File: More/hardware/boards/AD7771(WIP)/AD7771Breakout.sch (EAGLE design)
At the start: 44 parts, among them U1 AD7771BCPZ, U2 MAX6070AAUT25T, U3 LP5907MFX-3.3/NOPB, U4 TBA1-0310, U5 SG-210STF8.1920ML3, X1 332-02

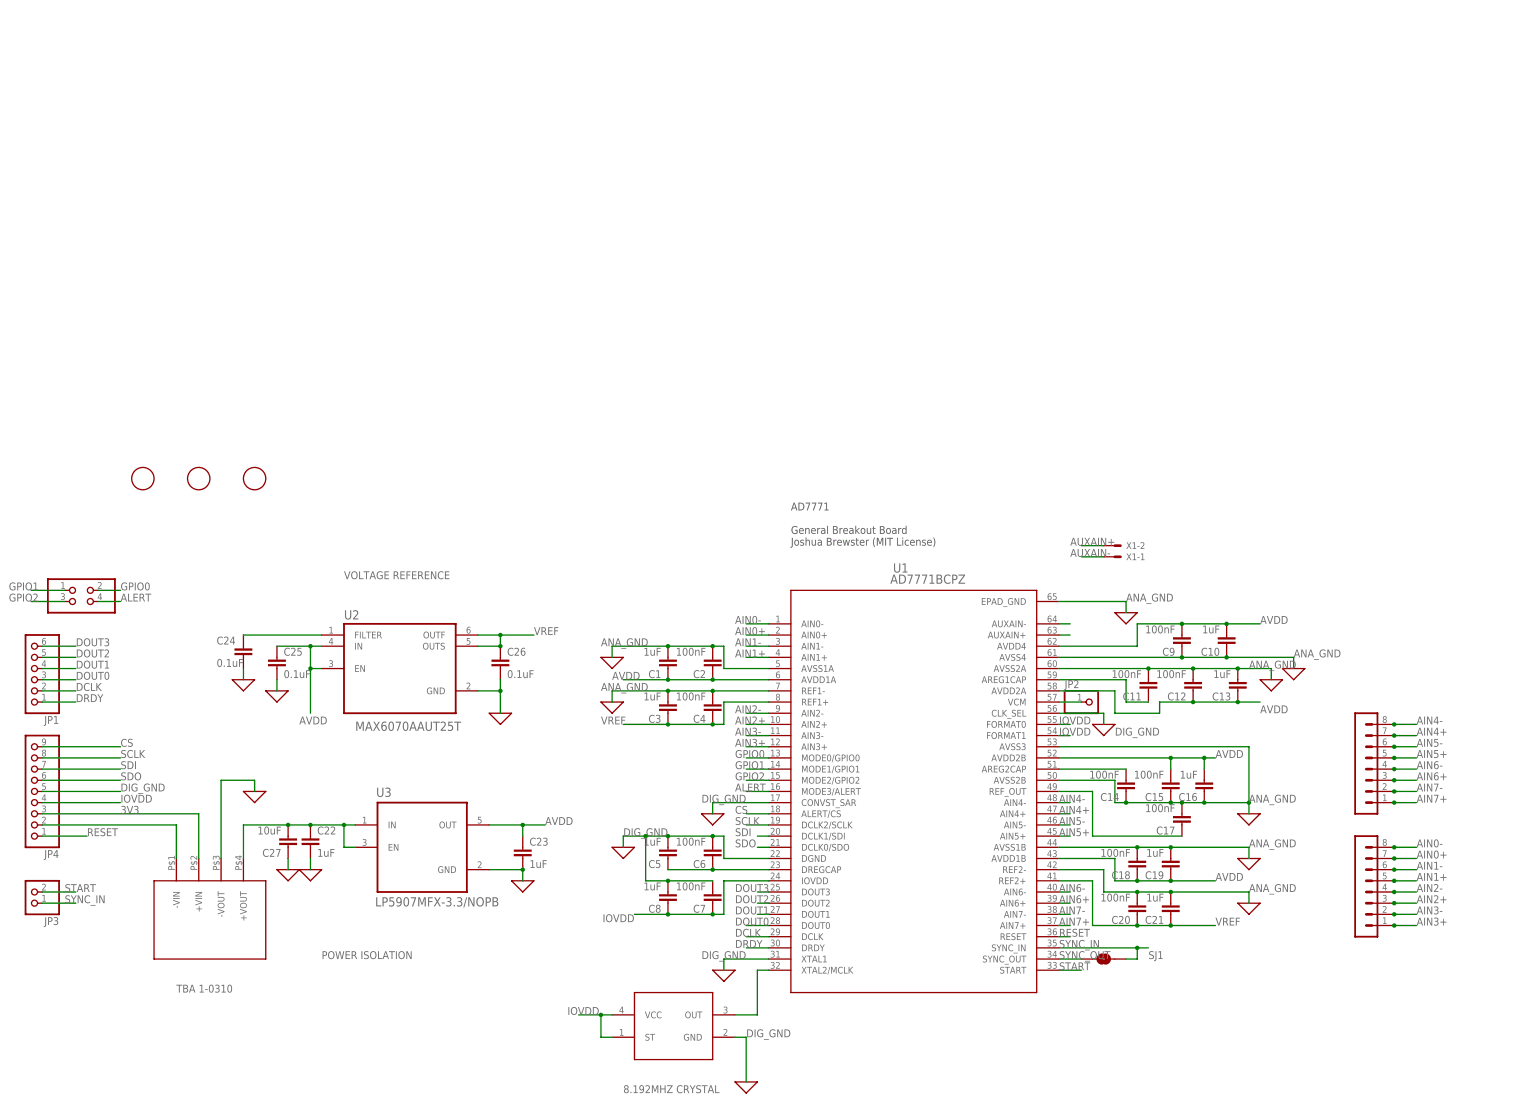
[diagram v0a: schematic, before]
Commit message: update schematic
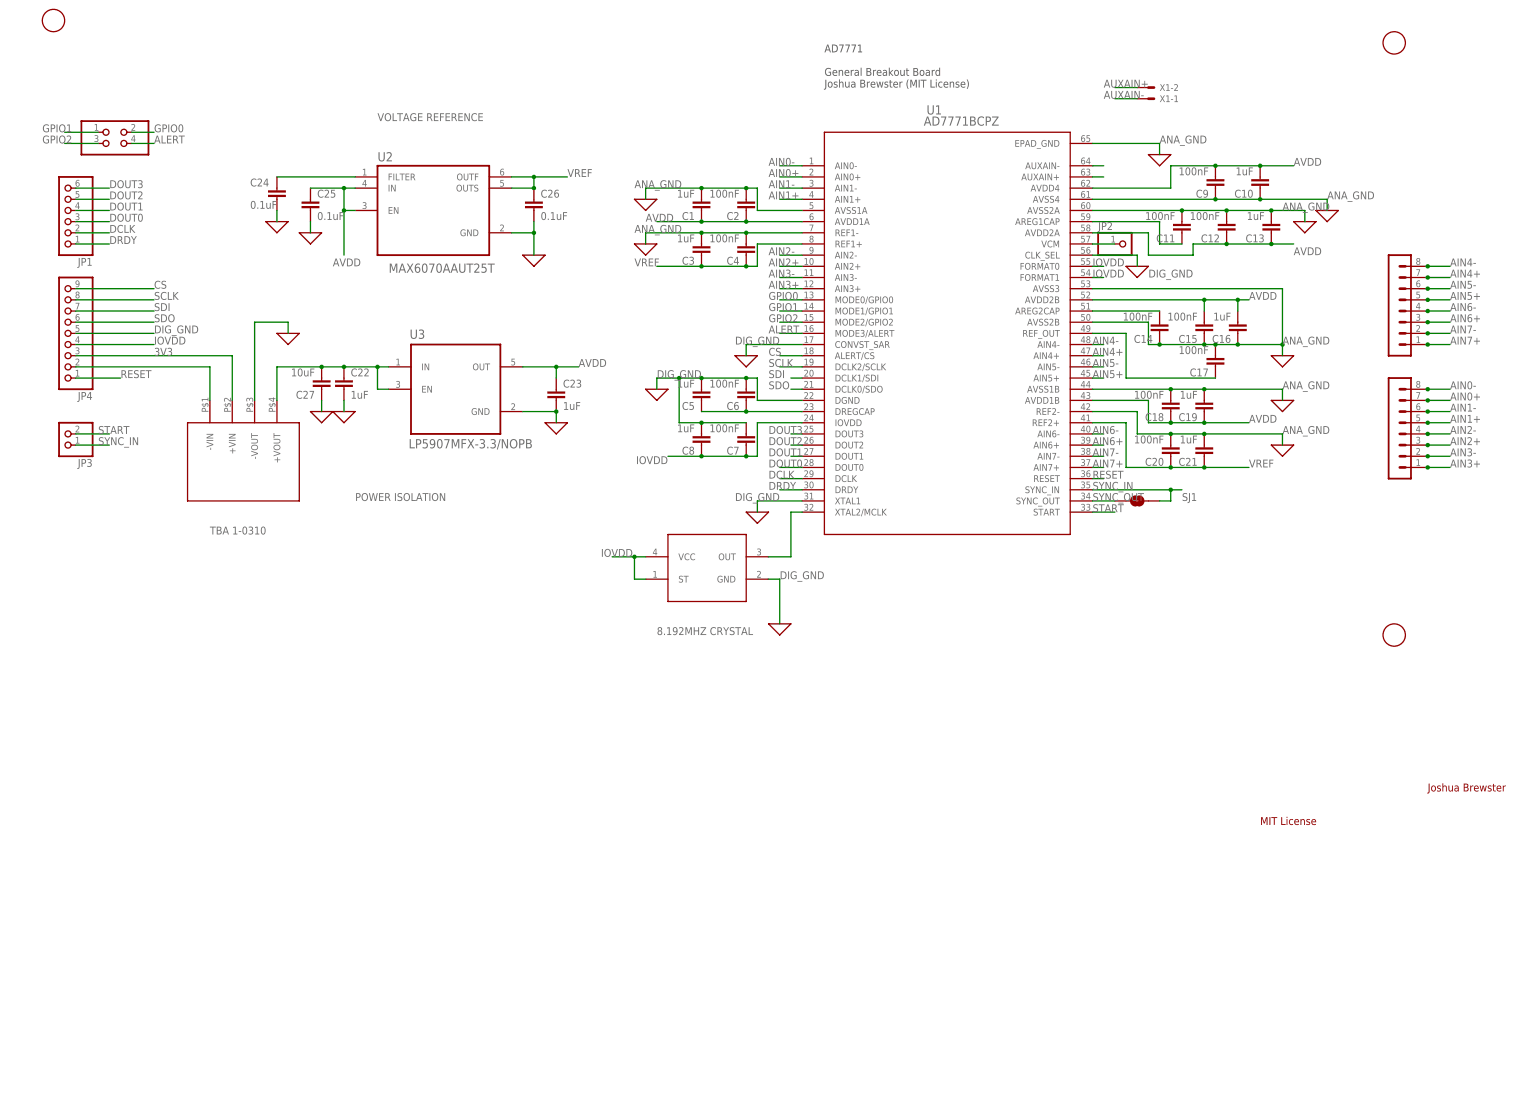
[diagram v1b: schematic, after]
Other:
- note added: "Joshua Brewster"
- note added: "MIT License"
- moved on the sheet: C1, C10, C11, C12, C13, C14, C15, C16, C17, C18, C19, C2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
